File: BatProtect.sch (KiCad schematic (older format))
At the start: 23 parts, among them J1 Bat, J2 Load, Q1 Q_PMOS_GDS, Q2 SI2308, SW1 SW_DIP_x01, U1 ATTINY13A, U2 MIC5219-5.0

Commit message: Adjust wierd problem in schematic and add firmware
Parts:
- Q2: footprint (none) -> TO_SOT_Packages_SMD:SOT-23
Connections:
- net GND: now also Q2.2 (S); no longer Q2.3 (D)
- net at R8.2: now also Q2.3 (D); no longer Q2.2 (S)
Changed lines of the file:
@@
 F 0 "Q2" H 5550 3550 50  0000 L CNN
 F 1 "SI2308" H 5550 3450 50  0000 L CNN
-F 2 "" H 5550 3600 50  0001 C CNN
+F 2 "TO_SOT_Packages_SMD:SOT-23" H 5550 3600 50  0001 C CNN
 F 3 "" H 5350 3500 50  0001 C CNN
 	1    5350 3500
-	-1   0    0    1
+	-1   0    0    -1
 $EndComp
 $EndSCHEMATC

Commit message: Again wierd bug in the schematic fixed
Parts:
- removed U1: ATTINY13A, Housings_SOIC:SOIC-8_3.9x4.9mm_Pitch1.27mm, symbol ATTINY15-1SC
- added U1: ATTINY13A-SU, Housings_SOIC:SOIC-8_3.9x4.9mm_Pitch1.27mm, symbol ATTINY13A-SU
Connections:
- net GND: now also U1.4 (GND)
- net at R5.1: now also U1.2 (PB3(CLKI/ADC3/PCINT3))
- net at R7.2: now also U1.1 (PB5(~RESET~/ADC0/PCINT5/dW))
- net at R3.2, R4.1: now also U1.3 (PB4(ADC2/PCINT4))
- net at D3.2 (A): now also U1.5 (PB0(MOSI/AIN0/OC0A/PCINT0))
- net at R6.2: now also U1.7 (PB2(SCK/ADC1/T0/PCINT2))
- net at C2.1, C3.1, R7.1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: now also U1.8 (VCC)
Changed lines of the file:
@@
 LIBS:contrib
 LIBS:valves
+LIBS:Attiny13a
 LIBS:BatProtect-cache
 EELAYER 25 0
@@
 $EndComp
 $Comp
-L ATTINY15-1SC U1
-U 1 1 59C3B7E7
-P 7600 3450
-F 0 "U1" H 6800 3850 50  0000 C CNN
-F 1 "ATTINY13A" H 8100 3050 50  0000 C CNN
-F 2 "Housings_SOIC:SOIC-8_3.9x4.9mm_Pitch1.27mm" H 8200 3450 50  0001 C CIN
-F 3 "" H 6800 3800 50  0001 C CNN
-	1    7600 3450
-	1    0    0    -1
-$EndComp
-$Comp
 L +BATT #PWR2
 U 1 1 59C3BDD2
@@
 	-1   0    0    -1
 $EndComp
+$Comp
+L ATTINY13A-SU U1
+U 1 1 59E8D549
+P 7600 3450
+F 0 "U1" H 6800 3850 50  0000 C CNN
+F 1 "ATTINY13A-SU" H 8150 3050 50  0000 C CNN
+F 2 "Housings_SOIC:SOIC-8_3.9x4.9mm_Pitch1.27mm" H 8250 3450 50  0001 C CIN
+F 3 "" H 6800 3800 50  0001 C CNN
+	1    7600 3450
+	1    0    0    -1
+$EndComp
 $EndSCHEMATC

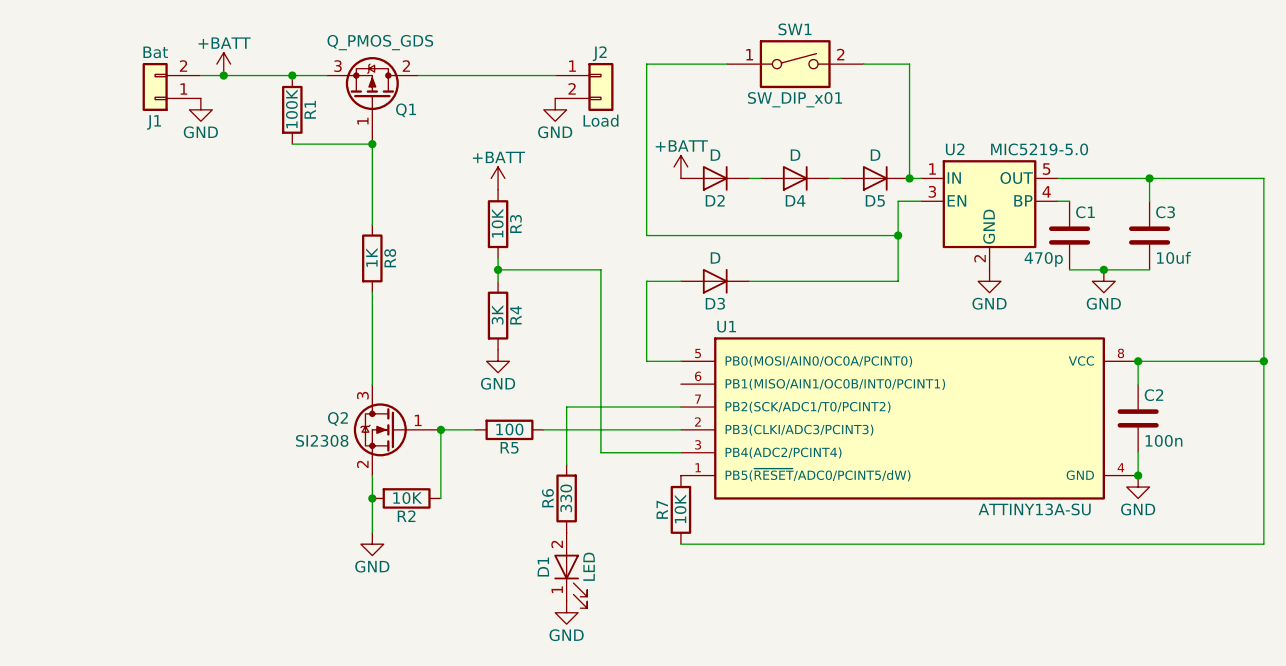
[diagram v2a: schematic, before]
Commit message: Adjust a bit schematic. Correct resistor divider
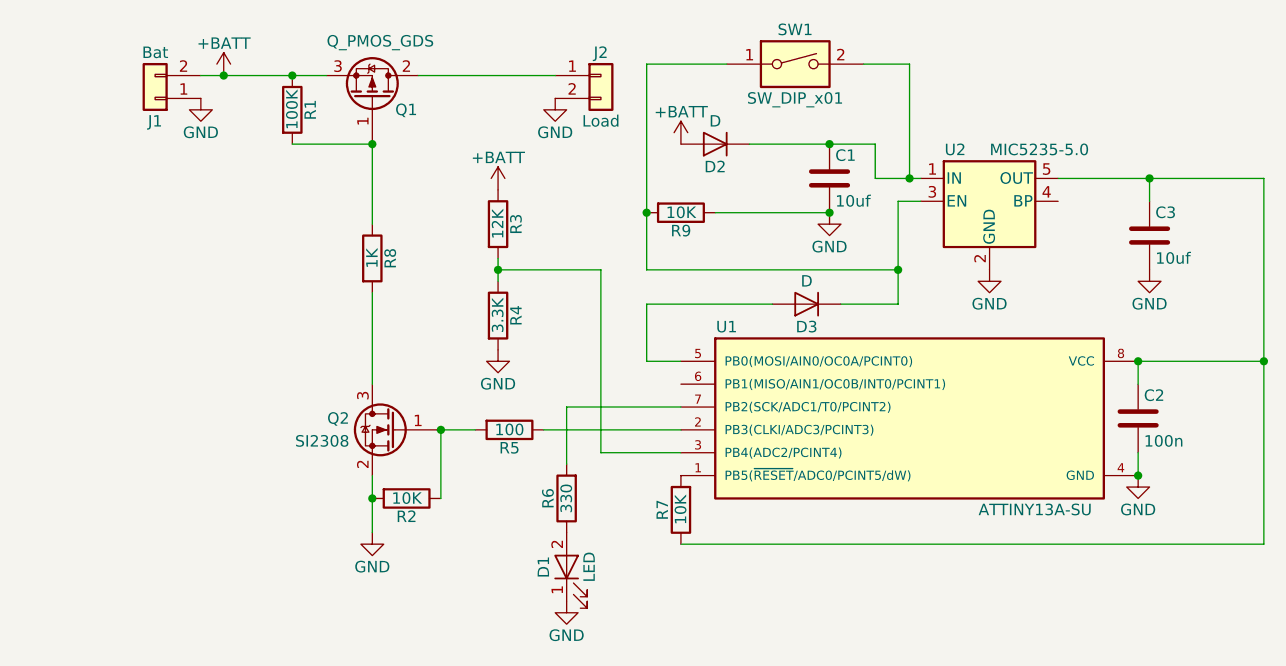
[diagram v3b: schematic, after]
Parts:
- removed D4, D5: D, Diodes_SMD:D_SOD-323_HandSoldering, symbol D
- added R9: 10K, Resistors_SMD:R_0603_HandSoldering, symbol R
- C1: value 470p -> 10uf
- R3: value 10K -> 12K
- R4: value 3K -> 3.3K
- U2: value MIC5219-5.0 -> MIC5235-5.0
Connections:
- net GND: now also R9.1
- net at SW1.2, U2.1 (IN): now also C1.1, D2.1 (K)
- net at D3.1 (K), SW1.1, U2.3 (EN): now also R9.2
- net at U2.4 (BP): no longer C1.1
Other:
- moved on the sheet: D2, D3
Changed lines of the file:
@@
 LIBS:contrib
 LIBS:valves
-LIBS:Attiny13a
 LIBS:BatProtect-cache
 EELAYER 25 0
@@
 P 5800 2600
 F 0 "R3" V 5880 2600 50  0000 C CNN
-F 1 "10K" V 5800 2600 50  0000 C CNN
+F 1 "12K" V 5800 2600 50  0000 C CNN
 F 2 "Resistors_SMD:R_0603_HandSoldering" V 5730 2600 50  0001 C CNN
 F 3 "" H 5800 2600 50  0001 C CNN
@@
 P 5800 3000
 F 0 "R4" V 5880 3000 50  0000 C CNN
-F 1 "3K" V 5800 3000 50  0000 C CNN
+F 1 "3.3K" V 5800 3000 50  0000 C CNN
 F 2 "Resistors_SMD:R_0603_HandSoldering" V 5730 3000 50  0001 C CNN
 F 3 "" H 5800 3000 50  0001 C CNN
@@
 P 7950 2500
 F 0 "U2" H 7800 2725 50  0000 C CNN
-F 1 "MIC5219-5.0" H 7950 2725 50  0000 L CNN
+F 1 "MIC5235-5.0" H 7950 2725 50  0000 L CNN
 F 2 "TO_SOT_Packages_SMD:SOT-23-5" H 7950 2825 50  0001 C CNN
 F 3 "" H 7950 2500 50  0001 C CNN
@@
 $EndComp
 $Comp
-L GND #PWR9
+L GND #PWR10
 U 1 1 59C3C847
 P 7950 2800
-F 0 "#PWR9" H 7950 2550 50  0001 C CNN
+F 0 "#PWR10" H 7950 2550 50  0001 C CNN
 F 1 "GND" H 7950 2650 50  0000 C CNN
 F 2 "" H 7950 2800 50  0001 C CNN
@@
 $EndComp
 $Comp
-L D D5
-U 1 1 59C3CA16
-P 7450 2400
-F 0 "D5" H 7450 2500 50  0000 C CNN
-F 1 "D" H 7450 2300 50  0000 C CNN
-F 2 "Diodes_SMD:D_SOD-323_HandSoldering" H 7450 2400 50  0001 C CNN
-F 3 "" H 7450 2400 50  0001 C CNN
-	1    7450 2400
-	-1   0    0    1
-$EndComp
-$Comp
-L D D4
-U 1 1 59C3CA8B
-P 7100 2400
-F 0 "D4" H 7100 2500 50  0000 C CNN
-F 1 "D" H 7100 2300 50  0000 C CNN
-F 2 "Diodes_SMD:D_SOD-323_HandSoldering" H 7100 2400 50  0001 C CNN
-F 3 "" H 7100 2400 50  0001 C CNN
-	1    7100 2400
-	-1   0    0    1
-$EndComp
-$Comp
 L D D2
 U 1 1 59C3CB00
-P 6750 2400
-F 0 "D2" H 6750 2500 50  0000 C CNN
-F 1 "D" H 6750 2300 50  0000 C CNN
-F 2 "Diodes_SMD:D_SOD-323_HandSoldering" H 6750 2400 50  0001 C CNN
-F 3 "" H 6750 2400 50  0001 C CNN
-	1    6750 2400
+P 6750 2250
+F 0 "D2" H 6750 2350 50  0000 C CNN
+F 1 "D" H 6750 2150 50  0000 C CNN
+F 2 "Diodes_SMD:D_SOD-323_HandSoldering" H 6750 2250 50  0001 C CNN
+F 3 "" H 6750 2250 50  0001 C CNN
+	1    6750 2250
 	-1   0    0    1
 $EndComp
@@
 L +BATT #PWR8
 U 1 1 59C3CB6E
-P 6600 2400
-F 0 "#PWR8" H 6600 2250 50  0001 C CNN
-F 1 "+BATT" H 6600 2540 50  0000 C CNN
-F 2 "" H 6600 2400 50  0001 C CNN
-F 3 "" H 6600 2400 50  0001 C CNN
-	1    6600 2400
+P 6600 2250
+F 0 "#PWR8" H 6600 2100 50  0001 C CNN
+F 1 "+BATT" H 6600 2390 50  0000 C CNN
+F 2 "" H 6600 2250 50  0001 C CNN
+F 3 "" H 6600 2250 50  0001 C CNN
+	1    6600 2250
 	1    0    0    -1
 $EndComp
@@
 L D D3
 U 1 1 59C3D1B2
-P 6750 2850
-F 0 "D3" H 6750 2950 50  0000 C CNN
-F 1 "D" H 6750 2750 50  0000 C CNN
-F 2 "Diodes_SMD:D_SOD-323_HandSoldering" H 6750 2850 50  0001 C CNN
-F 3 "" H 6750 2850 50  0001 C CNN
-	1    6750 2850
+P 7150 2950
+F 0 "D3" H 7150 3050 50  0000 C CNN
+F 1 "D" H 7150 2850 50  0000 C CNN
+F 2 "Diodes_SMD:D_SOD-323_HandSoldering" H 7150 2950 50  0001 C CNN
+F 3 "" H 7150 2950 50  0001 C CNN
+	1    7150 2950
 	-1   0    0    1
 $EndComp
@@
 Connection ~ 5800 2800
 Wire Wire Line
-	6900 2400 6950 2400
-Wire Wire Line
-	7250 2400 7300 2400
-Wire Wire Line
-	7600 2400 7650 2400
+	6900 2250 7450 2250
+Wire Wire Line
+	7450 2400 7650 2400
 Wire Wire Line
 	7650 2500 7550 2500
 Wire Wire Line
-	7550 2500 7550 2850
-Wire Wire Line
-	6450 2850 6450 3200
+	7550 2500 7550 2950
 Wire Wire Line
 	6450 3200 6600 3200
-Wire Wire Line
-	6450 2850 6600 2850
-Wire Wire Line
-	7550 2850 6900 2850
 Wire Wire Line
 	7400 1900 7600 1900
@@
 Connection ~ 7600 2400
 Wire Wire Line
-	7550 2650 6450 2650
-Wire Wire Line
-	6450 2650 6450 1900
+	7550 2800 6450 2800
+Wire Wire Line
+	6450 2800 6450 1900
 Wire Wire Line
 	6450 1900 6800 1900
-Connection ~ 7550 2650
+Connection ~ 7550 2800
 $Comp
 L C C2
@@
 $EndComp
 $Comp
-L C C1
-U 1 1 59C3D9FE
-P 8300 2650
-F 0 "C1" H 8325 2750 50  0000 L CNN
-F 1 "470p" H 8100 2550 50  0000 L CNN
-F 2 "Capacitors_SMD:C_0603_HandSoldering" H 8338 2500 50  0001 C CNN
-F 3 "" H 8300 2650 50  0001 C CNN
-	1    8300 2650
-	1    0    0    -1
-$EndComp
-$Comp
 L C C3
 U 1 1 59C3DB00
@@
 $EndComp
 Wire Wire Line
-	8300 2800 8650 2800
-Wire Wire Line
-	8250 2500 8300 2500
-Wire Wire Line
 	8250 2400 9150 2400
 Wire Wire Line
 	8650 2400 8650 2500
 $Comp
-L GND #PWR10
+L GND #PWR12
 U 1 1 59C3DC12
-P 8450 2800
-F 0 "#PWR10" H 8450 2550 50  0001 C CNN
-F 1 "GND" H 8450 2650 50  0000 C CNN
-F 2 "" H 8450 2800 50  0001 C CNN
-F 3 "" H 8450 2800 50  0001 C CNN
-	1    8450 2800
-	1    0    0    -1
-$EndComp
-Connection ~ 8450 2800
+P 8650 2800
+F 0 "#PWR12" H 8650 2550 50  0001 C CNN
+F 1 "GND" H 8650 2650 50  0000 C CNN
+F 2 "" H 8650 2800 50  0001 C CNN
+F 3 "" H 8650 2800 50  0001 C CNN
+	1    8650 2800
+	1    0    0    -1
+$EndComp
 Wire Wire Line
 	8600 3200 8600 3300
@@
 	1    0    0    -1
 $EndComp
+Wire Wire Line
+	7450 2250 7450 2400
+$Comp
+L C C1
+U 1 1 59F8B327
+P 7250 2400
+F 0 "C1" H 7275 2500 50  0000 L CNN
+F 1 "10uf" H 7275 2300 50  0000 L CNN
+F 2 "Capacitors_SMD:C_0603_HandSoldering" H 7288 2250 50  0001 C CNN
+F 3 "" H 7250 2400 50  0001 C CNN
+	1    7250 2400
+	1    0    0    -1
+$EndComp
+Connection ~ 7250 2250
+$Comp
+L GND #PWR9
+U 1 1 59F8B3C6
+P 7250 2550
+F 0 "#PWR9" H 7250 2300 50  0001 C CNN
+F 1 "GND" H 7250 2400 50  0000 C CNN
+F 2 "" H 7250 2550 50  0001 C CNN
+F 3 "" H 7250 2550 50  0001 C CNN
+	1    7250 2550
+	1    0    0    -1
+$EndComp
+Wire Wire Line
+	7550 2950 7300 2950
+Wire Wire Line
+	7000 2950 6450 2950
+Wire Wire Line
+	6450 2950 6450 3200
+$Comp
+L R R9
+U 1 1 59F8BC55
+P 6600 2550
+F 0 "R9" V 6680 2550 50  0000 C CNN
+F 1 "10K" V 6600 2550 50  0000 C CNN
+F 2 "Resistors_SMD:R_0603_HandSoldering" V 6530 2550 50  0001 C CNN
+F 3 "" H 6600 2550 50  0001 C CNN
+	1    6600 2550
+	0    1    1    0
+$EndComp
+Wire Wire Line
+	6750 2550 7250 2550
+Connection ~ 7250 2550
+Connection ~ 6450 2550
 $EndSCHEMATC

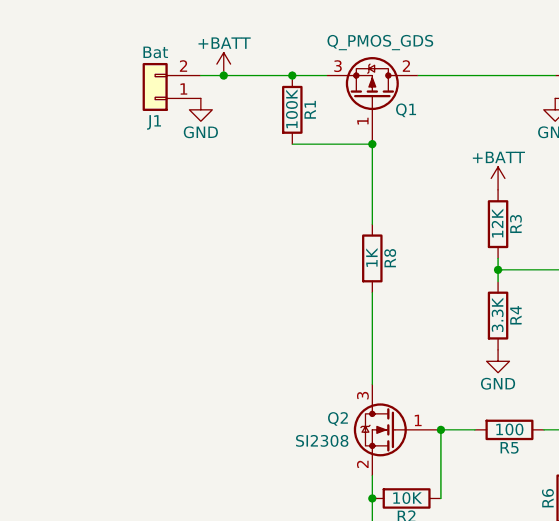
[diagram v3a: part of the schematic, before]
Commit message: ADC Vref changed from 5V to 1.1V
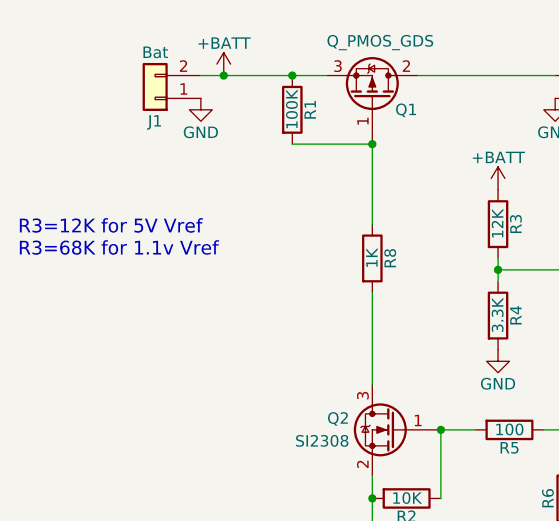
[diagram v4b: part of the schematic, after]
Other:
- note added: "R3=12K for 5V Vref\nR3=68K for 1.1v Vref"
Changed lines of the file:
@@
 Connection ~ 7250 2550
 Connection ~ 6450 2550
+Text Notes 3700 2750 0    60   ~ 0
+R3=12K for 5V Vref\nR3=68K for 1.1v Vref
 $EndSCHEMATC
